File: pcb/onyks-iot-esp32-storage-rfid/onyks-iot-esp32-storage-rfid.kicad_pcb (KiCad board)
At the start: 2 copper layers, 22 parts, among them J1 Conn_01x02_Pin, J2 Conn_01x06_Pin, J3 Conn_02x05_Top_Bottom, J5 Conn_01x03_Pin, J6 Conn_01x01_Pin, Q1 SS8050, Q2 SS8050, SW3 SW_Push, SW4 SW_Push, U1 ESP32-WROOM-32D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

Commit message: Zapomniałem o rulesach.
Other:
- copper layers 2 -> 4

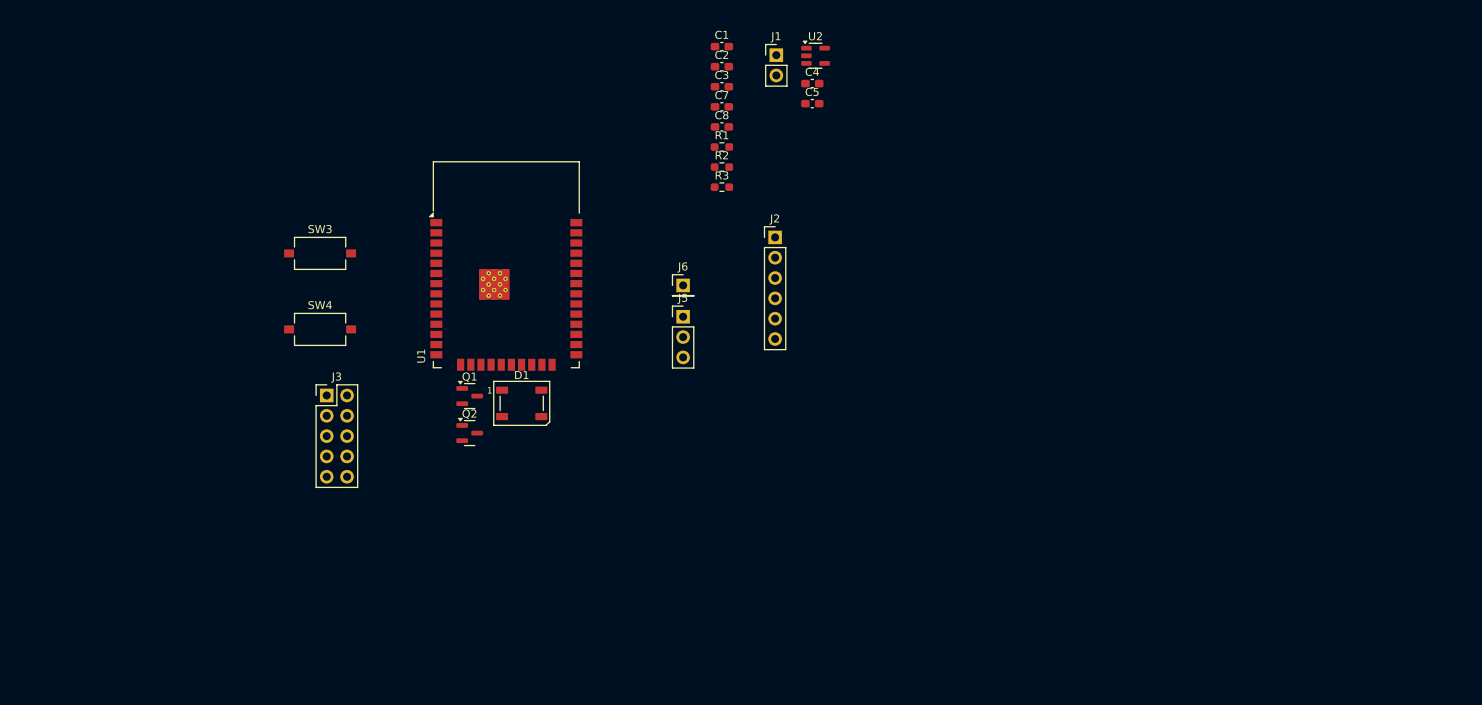
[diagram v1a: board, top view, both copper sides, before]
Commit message: oznaczenie pinów i podział elementów PCB
dodanie oznaczenia nieużywanych pinów zgodnie z opinią schematu
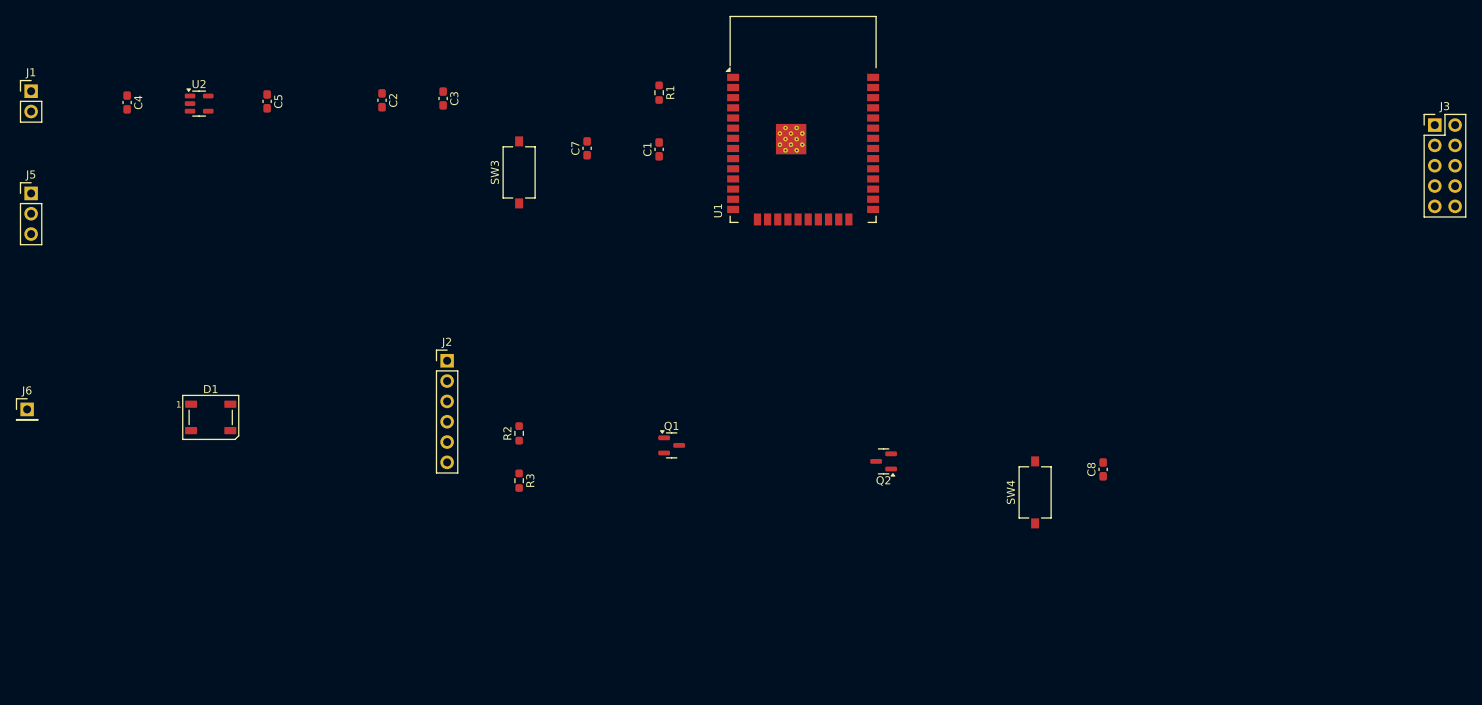
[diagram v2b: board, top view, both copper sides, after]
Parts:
- moved J3 142.6 mm to (240.5, 71.0)
- moved J1 93.3 mm to (65.0, 66.7)
- moved SW4 91.7 mm to (190.5, 116.9), turned to 90 degrees
- moved C4 85.7 mm to (77.0, 68.1), turned to -90 degrees
- moved J6 83.5 mm to (64.5, 106.5)
- moved J5 82.9 mm to (65.0, 79.5)
- moved U2 77.3 mm to (86.0, 68.3)
- moved C5 68.2 mm to (94.5, 68.0), turned to -90 degrees
- moved C8 64.1 mm to (199.0, 114.0), turned to 90 degrees
- moved Q2 51.9 mm to (171.6, 113.0), turned to 180 degrees
- moved R3 44.6 mm to (126.0, 115.4), turned to -90 degrees
- moved J2 43.8 mm to (117.0, 100.4)
- moved C2 42.7 mm to (108.9, 67.9), turned to -90 degrees
- moved R2 41.8 mm to (126.0, 109.5), turned to 90 degrees
- moved U1 41.3 mm to (161.5, 73.2)
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
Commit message: ustawienie i połączenia na PCB
szerokości ścieżek i wielkości przelotek jeszcze do poprawy
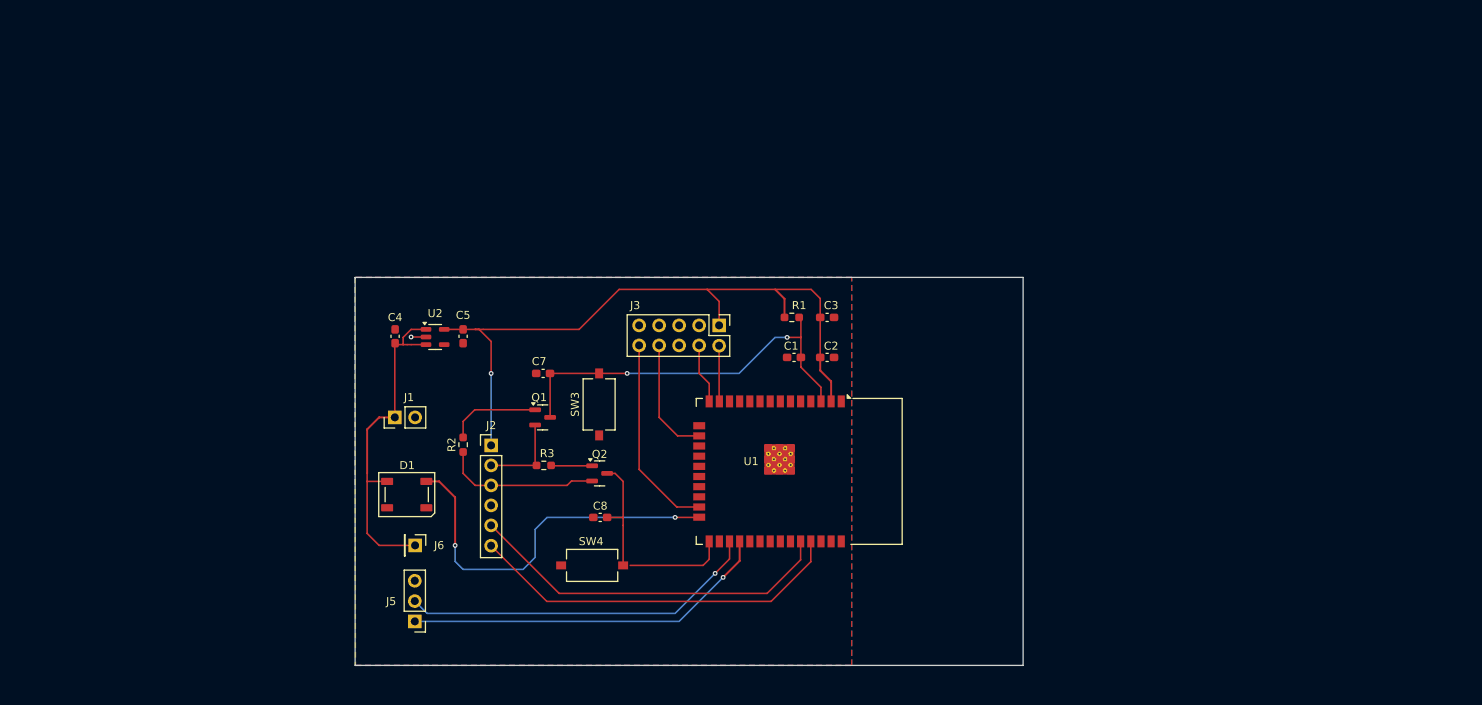
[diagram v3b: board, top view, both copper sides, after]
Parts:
- moved J3 92.9 mm to (151.0, 96.0), turned to -90 degrees
- moved J5 71.8 mm to (113.0, 133.0), turned to 180 degrees
- moved C2 64.3 mm to (164.5, 100.0), turned to 0 degrees
- moved C8 63.1 mm to (136.1, 120.0), turned to 0 degrees
- moved J1 61.1 mm to (110.5, 107.5), turned to 90 degrees
- moved SW4 56.1 mm to (135.1, 126.0), turned to 0 degrees
- moved C3 55.3 mm to (164.5, 95.0), turned to 0 degrees
- moved J6 51.4 mm to (113.0, 123.5), turned to -90 degrees
- moved C4 44.5 mm to (110.5, 97.4), turned to 90 degrees
- moved U2 41.5 mm to (115.5, 97.5)
- moved U1 41.2 mm to (158.0, 114.2), turned to -90 degrees
- moved C5 38.2 mm to (119.0, 97.4)
- moved Q2 35.5 mm to (136.1, 114.5), turned to 0 degrees
- moved R1 32.6 mm to (160.1, 95.0), turned to 0 degrees
- moved C1 31.0 mm to (160.4, 100.0), turned to 0 degrees
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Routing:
- net VDD33: track 0.00 -> 87.6 mm, vias 0 -> 1
- net /ESP32/EN: track 0.00 -> 50.0 mm, vias 0 -> 2
- net /ESP32/LED: track 0.00 -> 48.5 mm, vias 0 -> 2
- net /ESP32/PROGRAM_TXD: track 0.00 -> 47.4 mm
- net /ESP32/PROGRAM_RXD: track 0.00 -> 46.3 mm
- net /ESP32/TXD: track 0.00 -> 46.2 mm, vias 0 -> 1
- net /ESP32/RXD: track 0.00 -> 45.0 mm, vias 0 -> 1
- net VCC: track 0.00 -> 43.3 mm
- net /ESP32/IO0: track 0.00 -> 27.4 mm
- net /ESP32/MTDO: track 0.00 -> 25.0 mm
- net /ESP32/DTR: track 0.00 -> 19.6 mm
- net /ESP32/MTCK: track 0.00 -> 15.0 mm
- net Net-(Q1-B): track 0.00 -> 11.6 mm
- net /ESP32/RTS: track 0.00 -> 10.7 mm
- net /ESP32/MTDI: track 0.00 -> 7.52 mm
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- added copper zone on B.Cu, net GND
- added copper zone on F.Cu, net GND
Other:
- board outline added: 83.5 x 48.5 mm
- board text added: "J3"

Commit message: szerokości ścieżek
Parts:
- moved C8 6.15 mm to (137.5, 126.0)
- moved SW4 5.54 mm to (137.5, 121.0)
- moved J5 4.15 mm to (117.0, 132.0)
- moved D1 4.10 mm to (116.0, 117.2)
- moved J6 4.05 mm to (117.0, 123.2)
- moved C4 4.00 mm to (114.5, 97.5)
- moved C5 4.00 mm to (123.0, 97.4)
- moved J1 4.00 mm to (114.5, 107.5)
- moved J2 4.00 mm to (126.5, 111.0)
- moved U2 4.00 mm to (119.5, 97.5)
- moved R2 3.75 mm to (122.8, 110.9)
- moved C7 2.36 mm to (131.4, 102.0)
- moved Q1 2.12 mm to (131.1, 107.5)
- moved R3 2.00 mm to (131.1, 113.5)
- moved J3 1.50 mm to (152.5, 96.0)
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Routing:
- net /ESP32/LED: track 48.5 -> 44.1 mm
- net VDD33: track 87.6 -> 83.2 mm
- net /ESP32/RXD: track 45.0 -> 41.4 mm
- net /ESP32/TXD: track 46.2 -> 43.2 mm
- net /ESP32/EN: track 50.0 -> 47.5 mm
- net /ESP32/DTR: track 19.6 -> 17.5 mm
- net /ESP32/RTS: track 10.7 -> 8.68 mm
- net Net-(Q1-B): track 11.6 -> 9.98 mm
- net /ESP32/PROGRAM_RXD: track 46.3 -> 45.2 mm
- net /ESP32/PROGRAM_TXD: track 47.4 -> 46.5 mm
- net /ESP32/MTDO: track 25.0 -> 24.1 mm
- net /ESP32/MTCK: track 15.0 -> 14.1 mm
- net /ESP32/MTMS: track 6.97 -> 7.65 mm
- net Net-(Q2-B): track 5.15 -> 4.57 mm
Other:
- board size 83.5 x 48.5 mm -> 79.5 x 45.5 mm

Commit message: PCB gotowe do review
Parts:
- moved C4 4.10 mm to (110.7, 95.9)
- moved U2 2.33 mm to (117.7, 95.9)
- moved C5 2.19 mm to (121.4, 95.9)
- moved J3 1.89 mm to (150.9, 95.0)
- moved J5 1.07 mm to (116.8, 133.1)
- moved D1 0.89 mm to (115.7, 118.0)
- moved J6 0.78 mm to (116.8, 124.0)
- moved C1 0.70 mm to (159.7, 100.1)
- moved C2 0.57 mm to (163.9, 100.1)
- moved C3 0.57 mm to (163.9, 95.0)
- moved R2 0.55 mm to (122.4, 111.4)
- moved R1 0.47 mm to (159.6, 95.0)
- moved Q2 0.36 mm to (137.7, 114.8)
- moved R3 0.30 mm to (131.2, 113.8)
- moved J2 0.29 mm to (126.5, 111.3)
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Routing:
- net VCC: track 43.7 -> 52.8 mm
- net VDD33: track 83.2 -> 92.0 mm
- net /ESP32/RXD: track 41.4 -> 39.8 mm
- net /ESP32/MTDI: track 7.14 -> 8.57 mm
- net /ESP32/MTDO: track 24.1 -> 25.5 mm
- net /ESP32/PROGRAM_TXD: track 46.5 -> 47.6 mm
- net /ESP32/IO0: track 27.4 -> 26.6 mm
- net Net-(Q1-B): track 9.98 -> 10.6 mm
- net /ESP32/PROGRAM_RXD: track 45.2 -> 44.6 mm
- net /ESP32/TXD: track 43.2 -> 42.7 mm
- net /ESP32/EN: track 47.5 -> 48.0 mm
- net GND: track 1.86 -> 1.53 mm, vias 1 -> 10
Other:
- board size 79.5 x 45.5 mm -> 68.1 x 50.8 mm

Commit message: projekt PCB v2
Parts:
- removed J5: Conn_01x03_Pin, Connector_PinHeader_2.54mm:PinHeader_1x03_P2.54mm_Vertical
- removed J6: Conn_01x01_Pin, Connector_PinHeader_2.54mm:PinHeader_1x01_P2.54mm_Vertical
- added J4: Conn_01x04_Pin, Connector_PinHeader_2.54mm:PinHeader_1x04_P2.54mm_Vertical, F.Cu at (133.6, 120.7)
- added R4: 10k, Resistor_SMD:R_0603_1608Metric_Pad0.98x0.95mm_HandSolder, F.Cu at (130.8, 123.1)
- moved R2 38.8 mm to (151.3, 137.2), turned to 180 degrees
- moved J2 33.8 mm to (151.2, 134.4), turned to 90 degrees
- moved C7 31.6 mm to (145.6, 130.3), turned to 90 degrees
- moved Q1 30.1 mm to (150.8, 130.5), turned to 90 degrees
- moved R3 28.5 mm to (154.2, 130.5), turned to 90 degrees
- moved SW3 27.7 mm to (142.4, 133.3)
- moved Q2 25.3 mm to (157.5, 130.6)
- moved D1 24.5 mm to (139.8, 113.2)
- moved C4 23.0 mm to (133.6, 98.5)
- moved U2 21.3 mm to (138.9, 98.5)
- moved C5 20.8 mm to (142.0, 98.5)
- moved J1 19.4 mm to (133.6, 105.6)
- moved C8 8.29 mm to (145.6, 125.7), turned to -90 degrees
- moved SW4 5.37 mm to (142.4, 122.7), turned to -90 degrees
- moved J3 5.00 mm to (155.1, 97.7)
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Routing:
- net /ESP32/PROGRAM_TXD: track 47.6 -> 11.9 mm
- net /ESP32/PROGRAM_RXD: track 44.6 -> 11.4 mm
- net /ESP32/LED: track 43.7 -> 13.4 mm, vias 2 -> 0
- net /ESP32/EN: track 48.0 -> 67.3 mm
- net /ESP32/RXD: track 39.8 -> 21.2 mm, vias 1 -> 2
- net /ESP32/TXD: track 42.7 -> 26.0 mm, vias 1 -> 2
- net VDD33: track 92.0 -> 76.0 mm
- net VCC: track 52.8 -> 37.0 mm
- net /ESP32/DTR: track 17.8 -> 9.19 mm
- net /ESP32/MTDO: track 25.5 -> 20.5 mm
- net /ESP32/MTDI: track 8.57 -> 5.06 mm
- net /ESP32/RTS: track 8.85 -> 5.56 mm
- net /ESP32/MTCK: track 14.3 -> 11.7 mm
- net Net-(Q2-B): track 4.66 -> 2.40 mm
- net /ESP32/MTMS: track 7.85 -> 5.98 mm
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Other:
- board size 68.1 x 50.8 mm -> 46.8 x 48 mm

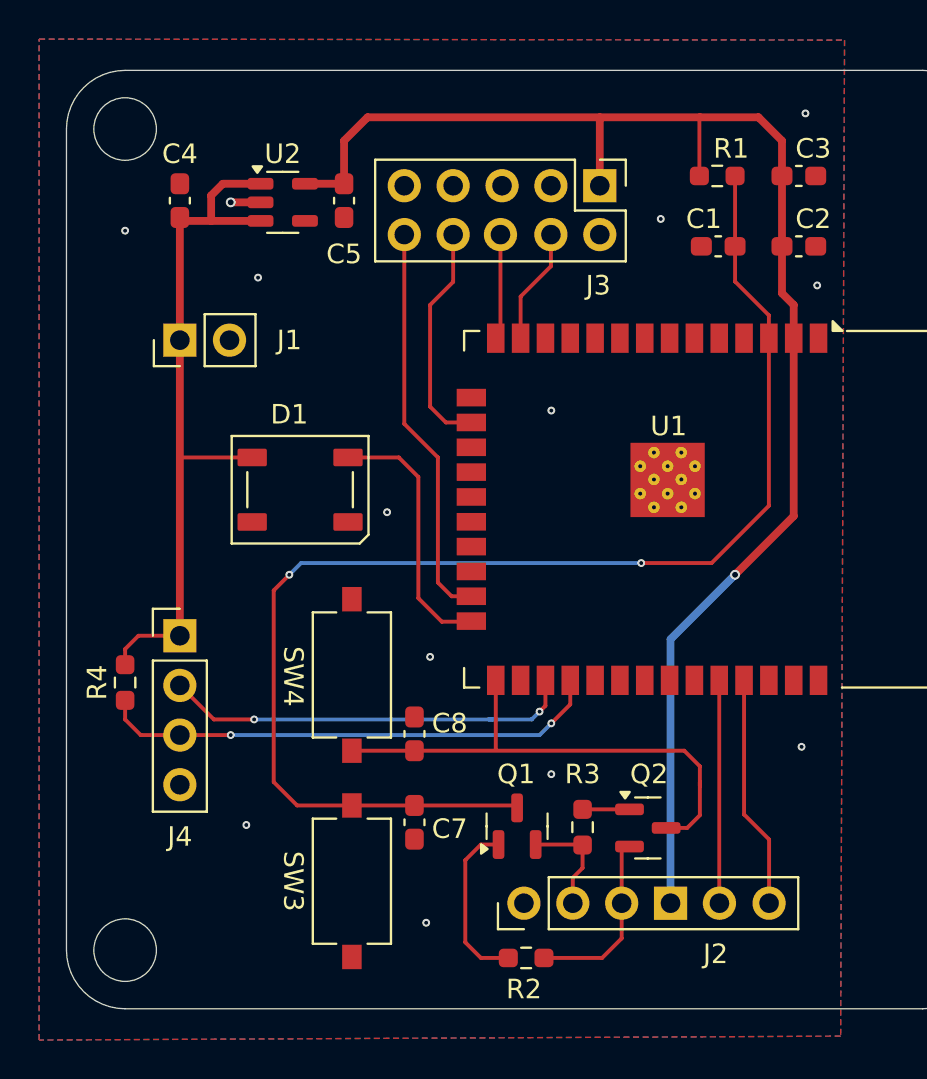
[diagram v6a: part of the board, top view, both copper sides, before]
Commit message: projekt PCB v2.2
Projekt gotowy do review. @przemech @Xenon02
Dodany zostal drugi stabilizator AMS1117-3.3, ktory mamy w nadmiarze w kole.
Zaktualizowano DR na zgodne z JLCPCB capabilities, ktore wczesniej byly bledne.
Dodano opis wymiarow plytki.
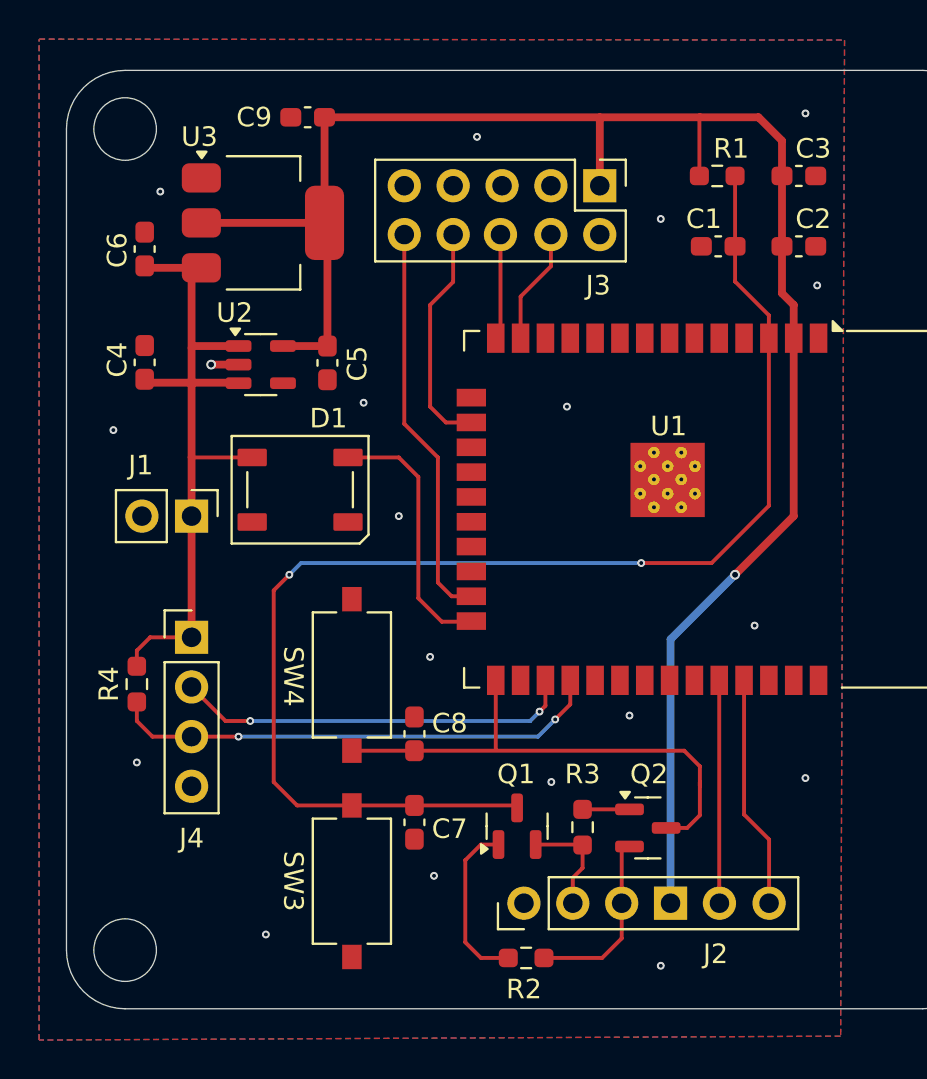
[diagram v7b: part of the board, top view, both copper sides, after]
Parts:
- added C6: 22uF/10VDC, Capacitor_SMD:C_0603_1608Metric_Pad1.08x0.95mm_HandSolder, F.Cu at (131.8, 100.9)
- added C9: 22uF/10VDC, Capacitor_SMD:C_0603_1608Metric_Pad1.08x0.95mm_HandSolder, F.Cu at (140.1, 94.2)
- added U3: AMS1117-3.3, Package_TO_SOT_SMD:SOT-223-3_TabPin2, F.Cu at (137.8, 99.6)
- moved J1 9.02 mm to (134.2, 114.6), turned to -90 degrees
- moved C4 8.47 mm to (131.8, 106.7)
- moved U2 8.38 mm to (137.7, 106.8)
- moved C5 8.34 mm to (141.2, 106.8)
- moved J4 0.61 mm to (134.2, 120.8)
- moved R4 0.61 mm to (131.4, 123.2)
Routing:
- net VDD33: track 76.0 -> 92.4 mm
- net VCC: track 37.0 -> 34.9 mm
- net /ESP32/RXD: track 21.2 -> 20.4 mm
- net /ESP32/TXD: track 26.0 -> 25.4 mm
- net GND: track 1.53 -> 1.40 mm, vias 13 -> 19

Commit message: zrobione review, wprowadzone poprawki, czeka na ostatnie sprawdzenie jak prezes bedzie bardizej przytomny
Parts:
- moved R2 7.01 mm to (155.3, 131.4)
- moved C3 4.15 mm to (165.5, 101.3)
- moved C1 2.86 mm to (162.1, 103.5)
- moved C2 2.33 mm to (165.5, 103.1)
- moved Q2 1.77 mm to (157.6, 128.8)
- moved R3 1.74 mm to (154.3, 128.8)
- moved Q1 0.75 mm to (150.8, 129.7)
- moved C9 0.08 mm to (140.2, 94.2)
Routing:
- net /ESP32/EN: track 67.3 -> 49.4 mm
- net /ESP32/RTS: track 5.56 -> 11.0 mm
- net /ESP32/IO0: track 26.4 -> 21.8 mm
- net /ESP32/DTR: track 9.19 -> 4.60 mm
- net Net-(Q1-B): track 8.76 -> 5.52 mm
- net GND: vias 19 -> 99
